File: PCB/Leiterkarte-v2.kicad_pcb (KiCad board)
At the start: 4 copper layers, 70 x 70 mm, 59 parts

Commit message: PCB Version 2.1
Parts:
- removed 3.3V1: LD39150DT33, Package_TO_SOT_SMD:TO-252-3_TabPin2
- removed Cmax1: 1nF, Capacitor_SMD:C_0805_2012Metric
- removed Rlind1, Rrind1, Rrpm1: 40k, Resistor_SMD:R_0603_1608Metric
- removed Rlind2, Rrind2, Rrpm2, Rspd1, Rup1: 10k, Resistor_SMD:R_0603_1608Metric
- removed Rspd2: 20k, Resistor_SMD:R_0603_1608Metric
- removed VRCond1: MAX9924UAUB_T, MAX9924UAUB:SOP50P490X110-10N
- added Cf1: spare, Capacitor_SMD:C_0805_2012Metric, F.Cu at (157.5, 91.5)
- added Cf10: C, Capacitor_SMD:C_0805_2012Metric, F.Cu at (124.0, 85.0)
- added Cf12: C, Capacitor_SMD:C_0805_2012Metric, F.Cu at (124.0, 88.0)
- added Cf13: C, Capacitor_SMD:C_0805_2012Metric, F.Cu at (124.0, 76.0)
- added Cf16: C, Capacitor_SMD:C_0805_2012Metric, F.Cu at (124.0, 79.0)
- added Cf3: spare, Capacitor_SMD:C_0805_2012Metric, F.Cu at (159.8, 91.5)
- added Cf5: C, Capacitor_SMD:C_0805_2012Metric, F.Cu at (125.0, 92.0)
- added Cf6: C, Capacitor_SMD:C_0805_2012Metric, F.Cu at (122.5, 92.0)
- added Cf8: C, Capacitor_SMD:C_0805_2012Metric, F.Cu at (124.0, 82.0)
- added Cin1.1: C, Capacitor_SMD:C_0805_2012Metric, F.Cu at (87.5, 99.0)
- added Cin2.1: C, Capacitor_SMD:C_0805_2012Metric, F.Cu at (101.0, 79.5)
- added Cout1.1: C, Capacitor_SMD:C_0805_2012Metric, F.Cu at (91.0, 73.0)
- added Cout2.1: C, Capacitor_SMD:C_0805_2012Metric, F.Cu at (102.5, 85.5)
- added D2: D_Schottky, Diode_SMD:D_0805_2012Metric, F.Cu at (159.8, 104.2)
- added D3: D_Schottky, Diode_SMD:D_0805_2012Metric, F.Cu at (159.0, 112.5)
- added D4: D_Schottky, Diode_SMD:D_0805_2012Metric, F.Cu at (159.0, 108.0)
- added D5: D_Zener 3.3V, Diode_SMD:D_0805_2012Metric, F.Cu at (170.0, 103.0)
- added D6: D_Schottky, Diode_SMD:D_0805_2012Metric, F.Cu at (163.8, 104.2)
- added D7: D_Zener 3.3V, Diode_SMD:D_0805_2012Metric, F.Cu at (157.5, 69.5)
- added D8: D_Zener 3.3V, Diode_SMD:D_0805_2012Metric, F.Cu at (157.5, 74.2)
- added JP1: SolderJumper_2_Open, Jumper:SolderJumper-2_P1.3mm_Open_TrianglePad1.0x1.5mm, F.Cu at (107.0, 57.5)
- added R10: 100k, Resistor_SMD:R_0805_2012Metric, F.Cu at (165.0, 112.5)
- added R11: 100k, Resistor_SMD:R_0805_2012Metric, F.Cu at (165.0, 108.0)
- added R12: spare, Resistor_SMD:R_0805_2012Metric, F.Cu at (162.0, 91.5)
- added R13: 10k, Resistor_SMD:R_0805_2012Metric, F.Cu at (167.2, 103.0)
- added R3: 100k, Resistor_SMD:R_0805_2012Metric, F.Cu at (157.6, 95.7)
- added R4: 10k, Resistor_SMD:R_0805_2012Metric, F.Cu at (160.4, 95.7)
- added R5: 10k, Resistor_SMD:R_0805_2012Metric, F.Cu at (173.8, 103.2)
- added R6: 10k, Resistor_SMD:R_0805_2012Metric, F.Cu at (161.0, 73.2)
- added R7: 10k, Resistor_SMD:R_0805_2012Metric, F.Cu at (161.1, 70.5)
- added R8: 40k, Resistor_SMD:R_0805_2012Metric, F.Cu at (164.6, 69.4)
- added R9: 40k, Resistor_SMD:R_0805_2012Metric, F.Cu at (164.6, 74.4)
- added TP1: TestPoint_Small, TestPoint:TestPoint_Pad_D1.0mm, F.Cu at (83.5, 101.2)
- added TP10: TestPoint_Small, TestPoint:TestPoint_Pad_D1.0mm, F.Cu at (162.0, 76.0)
- added TP11: TestPoint_Small, TestPoint:TestPoint_Pad_D1.0mm, F.Cu at (162.0, 67.5)
- added TP12: TestPoint_Small, TestPoint:TestPoint_Pad_D1.0mm, F.Cu at (164.2, 102.2)
- added TP13: TestPoint_Small, TestPoint:TestPoint_Pad_D1.0mm, F.Cu at (109.5, 60.2)
- added TP14: TestPoint_Small, TestPoint:TestPoint_Pad_D1.0mm, F.Cu at (109.5, 64.8)
- added TP15: TestPoint_Small, TestPoint:TestPoint_Pad_D1.0mm, F.Cu at (140.0, 99.5)
- added TP16: TestPoint_Small, TestPoint:TestPoint_Pad_D1.0mm, F.Cu at (142.5, 100.5)
- added TP18: TestPoint_Small, TestPoint:TestPoint_Pad_D1.0mm, F.Cu at (144.8, 97.8)
- added TP19: TestPoint_Small, TestPoint:TestPoint_Pad_D1.0mm, F.Cu at (148.2, 99.5)
- added TP20: TestPoint_Small, TestPoint:TestPoint_Pad_D1.0mm, F.Cu at (151.5, 101.0)
- added TP21: TestPoint_Small, TestPoint:TestPoint_Pad_D1.0mm, F.Cu at (145.0, 101.0)
- added TP22: TestPoint_Small, TestPoint:TestPoint_Pad_D1.0mm, F.Cu at (137.0, 100.5)
- added TP23: TestPoint_Small, TestPoint:TestPoint_Pad_D1.0mm, F.Cu at (134.8, 99.0)
- added TP24: TestPoint_Small, TestPoint:TestPoint_Pad_D1.0mm, F.Cu at (128.8, 63.5)
- added TP25: TestPoint_Small, TestPoint:TestPoint_Pad_D1.0mm, F.Cu at (136.2, 72.8)
- added TP26: TestPoint_Small, TestPoint:TestPoint_Pad_D1.0mm, F.Cu at (133.5, 62.8)
- added TP27: TestPoint_Small, TestPoint:TestPoint_Pad_D1.0mm, F.Cu at (135.8, 64.8)
- added TP28: TestPoint_Small, TestPoint:TestPoint_Pad_D1.0mm, F.Cu at (124.0, 64.5)
- added TP29: TestPoint_Small, TestPoint:TestPoint_Pad_D1.0mm, F.Cu at (132.0, 69.8)
- added TP3: TestPoint_Small, TestPoint:TestPoint_Pad_D1.0mm, F.Cu at (118.8, 99.2)
- added TP30: TestPoint_Small, TestPoint:TestPoint_Pad_D1.0mm, F.Cu at (155.2, 73.2)
- added TP31: TestPoint_Small, TestPoint:TestPoint_Pad_D1.0mm, F.Cu at (154.1, 70.4)
- added TP32: TestPoint_Small, TestPoint:TestPoint_Pad_D1.0mm, F.Cu at (158.8, 99.8)
- added TP33: TestPoint_Small, TestPoint:TestPoint_Pad_D1.0mm, F.Cu at (117.0, 80.5)
- added TP34: TestPoint_Small, TestPoint:TestPoint_Pad_D1.0mm, F.Cu at (163.0, 94.8)
- added TP35: TestPoint_Small, TestPoint:TestPoint_Pad_D1.0mm, F.Cu at (161.8, 100.0)
- added TP36: TestPoint_Small, TestPoint:TestPoint_Pad_D1.0mm, F.Cu at (152.2, 87.5)
- added TP37: TestPoint_Small, TestPoint:TestPoint_Pad_D1.0mm, F.Cu at (152.8, 52.8)
- added TP38: TestPoint_Small, TestPoint:TestPoint_Pad_D1.0mm, F.Cu at (164.0, 50.0)
- added TP39: TestPoint_Small, TestPoint:TestPoint_Pad_D1.0mm, F.Cu at (111.8, 90.2)
- added TP4: TestPoint_Small, TestPoint:TestPoint_Pad_D1.0mm, F.Cu at (105.8, 88.2)
- added TP5: TestPoint_Small, TestPoint:TestPoint_Pad_D1.0mm, F.Cu at (88.8, 77.2)
- added TP7: TestPoint_Small, TestPoint:TestPoint_Pad_D1.0mm, F.Cu at (170.0, 88.8)
- added TP8: TestPoint_Small, TestPoint:TestPoint_Pad_D1.0mm, F.Cu at (173.0, 88.8)
- added TP9: TestPoint_Small, TestPoint:TestPoint_Pad_D1.0mm, F.Cu at (176.0, 88.8)
- added U1: LMV321, LMV321SEG-7:SOT65P210X110-5N, F.Cu at (154.5, 93.8)
- added V3.31: LD39150DT33, Package_TO_SOT_SMD:TO-252-3_TabPin2, F.Cu at (95.0, 82.3)
- 5V1, Cboot1, Cin1, Cin2, Cout1, D1, L1, Rfbb1, Rfbt1: moved to F.Cu
- Fan1, Indics1, Speed1: footprint Connector_JST:JST_SH_BM02B-SRSS-TB_1x02-1MP_P1.00mm_Vertical -> Connector_JST:JST_XH_S2B-XH-A_1x02_P2.50mm_Horizontal
- R1, R2: value 10k -> 40k
- Rfuel1, Roil1: value 100 -> 240
- Rwtr1: value 100 -> 3k
- SPI1, SPI2, SPI3: footprint Connector_JST:JST_SH_BM08B-SRSS-TB_1x08-1MP_P1.00mm_Vertical -> Connector_JST:JST_XH_S8B-XH-A_1x08_P2.50mm_Horizontal
- TEMP_S1: value MCP9700Ax-ETT -> Conn_01x03_Pin; footprint Package_TO_SOT_SMD:SOT-23 -> Connector_JST:JST_XH_S3B-XH-A_1x03_P2.50mm_Horizontal
- TEMP_S2: value Conn_01x03_Pin -> MCP9700Ax-ETT; footprint Connector_JST:JST_SH_BM03B-SRSS-TB_1x03-1MP_P1.00mm_Vertical -> Package_TO_SOT_SMD:SOT-23
- gauges1: footprint Connector_JST:JST_SH_BM03B-SRSS-TB_1x03-1MP_P1.00mm_Vertical -> Connector_JST:JST_XH_S3B-XH-A_1x03_P2.50mm_Horizontal
- moved Resp1 52.5 mm to (147.5, 64.5), turned to 180 degrees
- moved Cen1 47.6 mm to (143.0, 70.5)
- moved ESP_RST1 46.5 mm to (141.5, 66.0)
- moved TEMP_S1 42.1 mm to (170.1, 64.8), turned to 90 degrees
- moved G*** 42.0 mm to (114.5, 69.5)
- moved Rboot1 39.5 mm to (130.5, 97.0), turned to -90 degrees
- moved ESP_BOOT1 33.0 mm to (124.5, 96.0)
- moved ESP1 30.8 mm to (139.5, 84.2)
- moved Fan1 29.9 mm to (170.1, 53.8), turned to 90 degrees
- moved Rbtn3 29.4 mm to (167.8, 93.8), turned to 90 degrees
- moved Cout1 29.3 mm to (94.0, 73.0)
- moved Rbtn1 27.9 mm to (170.2, 93.8), turned to 90 degrees
- moved Buttons1 27.2 mm to (177.8, 98.0), turned to -90 degrees
- moved RPM1 26.8 mm to (177.8, 102.0), turned to 0 degrees
- moved Cin2 26.2 mm to (101.0, 77.0), turned to 0 degrees
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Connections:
- ESP1 pad 17: LIndicator -> RIndicator
- ESP1 pad 18: RIndicator -> LIndicator
- ESP1 pad 19: Fuel -> WTemp
- ESP1 pad 21: WTemp -> Fuel
- R2 pad 2: Net-(VRCond1-IN+) -> GND
- Rbtn2 pad 1: Button2 -> GND
- Rbtn2 pad 2: GND -> Button3
- Rbtn3 pad 1: GND -> Button2
- Rbtn3 pad 2: Button3 -> GND
- TEMP_S1 pad 1: +3.3V -> GND
- TEMP_S1 pad 2: TEMP1 -> TEMP2
- TEMP_S1 pad 3: GND -> +3.3V
- TEMP_S2 pad 1: GND -> +3.3V
- TEMP_S2 pad 2: TEMP2 -> TEMP1
- TEMP_S2 pad 3: +3.3V -> GND
- USBC1 pad A4_B9: unconnected-(USBC1-VBUS-PadA4_B9) -> Net-(JP1-A)
- USBC1 pad B4_A9: unconnected-(USBC1-VBUS__1-PadB4_A9) -> Net-(JP1-A)
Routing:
- net +3.3V: track 263.5 -> 47.0 mm, vias 22 -> 16
- net GND: track 80.3 -> 164.5 mm, vias 40 -> 71
- net Net-(Cshld1-Pad2): track 0.00 -> 42.9 mm
- net Button3: track 61.1 -> 25.3 mm, vias 0 -> 1
- net USB_D-: track 15.8 -> 50.5 mm, vias 0 -> 2
- net USB_D+: track 17.0 -> 49.7 mm, vias 0 -> 2
- net Speed: track 57.7 -> 29.2 mm
- net Button2: track 75.1 -> 47.0 mm, vias 0 -> 2
- net BL: track 60.5 -> 88.1 mm
- net Net-(5V1-PH): track 15.9 -> 43.0 mm
- net Button1: track 74.6 -> 50.6 mm, vias 0 -> 2
- net CS3: track 33.9 -> 14.1 mm
- net Net-(D2-K): track 14.4 -> 31.2 mm, vias 2 -> 0
- net RST: track 68.4 -> 84.3 mm
- net Net-(5V1-VSENSE): track 4.71 -> 20.4 mm, vias 0 -> 2
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- added copper zone on B.Cu, net +3.3V
- added copper zone on F.Cu, net +3.3V
- removed copper zone on B.Cu, net GND
- removed copper zone on F.Cu, net GND
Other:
- board size 70 x 70 mm -> 100 x 70 mm
- board text added: "+"
- board text added: "3.3V"
- board text added: "5V"
- board text added: "BOOT"
- board text added: "Buttons"
- board text added: "FAN"
- board text added: "INDIC"
- board text added: "L"
- board text added: "O"
- board text added: "P"
- board text added: "R"
- board text added: "RPM"
- board text added: "Reset"
- board text added: "SPEED"
- board text added: "SPI1"
- board text added: "SPI2"
- board text added: "TEMP2"
- board text added: "VCC"
- board text added: "W"
- board text added: "v2.1 - XX.03.2025"
- board text removed: "+-"
- board text removed: "-+"
- board text removed: "-O+"
- board text removed: "FOW"
- board text removed: "LR"
- board text removed: "v2.0 - 12.10.2024"

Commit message: Fixed wrong SPI label
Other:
- board text added: "SPI3"
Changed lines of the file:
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@@
 		)
 	)
-	(gr_text "SPI2"
+	(gr_text "SPI3"
 		(at 143.75 103.25 0)
 		(layer "F.SilkS" knockout)
@@
 		(min_thickness 0.25)
 		(filled_areas_thickness no)
-		(fill yes
+		(fill
 			(thermal_gap 0.5)
 			(thermal_bridge_width 0.5)
@@
 		(min_thickness 0.25)
 		(filled_areas_thickness no)
-		(fill yes
+		(fill
 			(thermal_gap 0.5)
 			(thermal_bridge_width 0.5)

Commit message: Redone Schematics for better readability (the circuitry didnt change
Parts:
- removed 5V1: TPS5430DDA, Package_SO:TI_SO-PowerPAD-8_ThermalVias
- removed Buttons1: Conn_01x06_Pin, Connector_PinHeader_2.54mm:PinHeader_1x06_P2.54mm_Vertical
- removed Cboot1: 10nF, Capacitor_SMD:C_0805_2012Metric
- removed Cen1, Cin2: 1uF, Capacitor_SMD:C_0805_2012Metric
- removed Cesp1, Cin1: 22uF, Capacitor_SMD:C_0805_2012Metric
- removed Cesp2: 0.1uF, Capacitor_SMD:C_0805_2012Metric
- removed Cf1, Cf3: spare, Capacitor_SMD:C_0805_2012Metric
- removed Cf10, Cf12, Cf13, Cf16, Cf5, Cf6, Cf8, Cin1.1, Cin2.1, Cout1.1, Cout2.1: C, Capacitor_SMD:C_0805_2012Metric
- removed Cout1: 2.2uF, Capacitor_SMD:C_0805_2012Metric
- removed Cout2: 220uF, Capacitor_SMD:CP_Elec_6.3x5.9
- removed Cshld1: 50nF, Capacitor_SMD:C_0805_2012Metric
- removed D1: 550mV 5A, Diode_SMD:D_SMA
- removed D2, D3, D4, D6: D_Schottky, Diode_SMD:D_0805_2012Metric
- removed D5, D7, D8: D_Zener 3.3V, Diode_SMD:D_0805_2012Metric
- removed ESP1: ESP32-S3-WROOM-1U, RF_Module:ESP32-S3-WROOM-1U
- removed ESP_BOOT1, ESP_RST1: SW_SPST, button:small_button
- removed F1: 2A, Fuse:Fuse_1206_3216Metric
- removed Fan1, Indics1, Speed1: Conn_01x02_Pin, Connector_JST:JST_XH_S2B-XH-A_1x02_P2.50mm_Horizontal
- removed GND1, Vcc1: Conn_01x01_Pin, MountingHole:MountingHole_3.2mm_M3_Pad
- removed JP1: SolderJumper_2_Open, Jumper:SolderJumper-2_P1.3mm_Open_TrianglePad1.0x1.5mm
- removed L1: SPM6530T 15uH, SPM6530T:IND_SPM6530T-150M-HZ
- removed Qfan1: 2N7002-HXY, Package_TO_SOT_SMD:SOT-23
- removed R1, R2, R8, R9: 40k, Resistor_SMD:R_0805_2012Metric
- removed R10, R11, R3: 100k, Resistor_SMD:R_0805_2012Metric
- removed R12: spare, Resistor_SMD:R_0805_2012Metric
- removed R13, R4, R5, R6, R7: 10k, Resistor_SMD:R_0805_2012Metric
- removed RPM1: Conn_01x01_Pin, Connector_PinHeader_2.54mm:PinHeader_1x01_P2.54mm_Vertical
- removed Rboot1, Rbtn1, Rbtn2, Rbtn3, Rfbt1: 10k, Resistor_SMD:R_0603_1608Metric
- removed Resp1, Rusb1, Rusb2: 5.1k, Resistor_SMD:R_0603_1608Metric
- removed Rfbb1: 3.24k, Resistor_SMD:R_0603_1608Metric
- removed Rfuel1, Roil1: 240, Resistor_SMD:R_0603_1608Metric
- removed Rwtr1: 3k, Resistor_SMD:R_0603_1608Metric
- removed SD1: MSD-1-A, MSD-1-A:CUI_MSD-1-A
- removed SPI1, SPI2, SPI3: Conn_01x08, Connector_JST:JST_XH_S8B-XH-A_1x08_P2.50mm_Horizontal
- removed TEMP_S1, gauges1: Conn_01x03_Pin, Connector_JST:JST_XH_S3B-XH-A_1x03_P2.50mm_Horizontal
- removed TEMP_S2: MCP9700Ax-ETT, Package_TO_SOT_SMD:SOT-23
- removed TP1, TP10, TP11, TP12, TP13, TP14, TP15, TP16, TP18, TP19, TP20, TP21, TP22, TP23, TP24, TP25, TP26, TP27, TP28, TP29, TP3, TP30, TP31, TP32, TP33, TP34, TP35, TP36, TP37, TP38, TP39, TP4, TP5, TP7, TP8, TP9: TestPoint_Small, TestPoint:TestPoint_Pad_D1.0mm
- removed U1: LMV321, LMV321SEG-7:SOT65P210X110-5N
- removed USBC1: USB4105-GF-A, USB-C 2.0:GCT_USB4105-GF-A
- removed V3.31: LD39150DT33, Package_TO_SOT_SMD:TO-252-3_TabPin2
- added 5V301: TPS5430DDA, Package_SO:TI_SO-PowerPAD-8_ThermalVias, F.Cu at (94.1, 96.3)
- added Buttons601: Conn_01x06_Pin, Connector_PinHeader_2.54mm:PinHeader_1x06_P2.54mm_Vertical, F.Cu at (177.8, 98.0)
- added C401: C, Capacitor_SMD:C_0805_2012Metric, F.Cu at (122.5, 92.0)
- added C402: C, Capacitor_SMD:C_0805_2012Metric, F.Cu at (124.0, 79.0)
- added C403: C, Capacitor_SMD:C_0805_2012Metric, F.Cu at (124.0, 76.0)
- added C404: C, Capacitor_SMD:C_0805_2012Metric, F.Cu at (125.0, 92.0)
- added C405: C, Capacitor_SMD:C_0805_2012Metric, F.Cu at (124.0, 82.0)
- added C406: C, Capacitor_SMD:C_0805_2012Metric, F.Cu at (124.0, 85.0)
- added C407: C, Capacitor_SMD:C_0805_2012Metric, F.Cu at (124.0, 88.0)
- added C501: C, Capacitor_SMD:C_0805_2012Metric, F.Cu at (157.5, 91.5)
- added C502: C, Capacitor_SMD:C_0805_2012Metric, F.Cu at (159.8, 91.5)
- added Cboot301: 10nF, Capacitor_SMD:C_0805_2012Metric, F.Cu at (97.0, 89.0)
- added Cen201: 1uF, Capacitor_SMD:C_0805_2012Metric, F.Cu at (143.0, 70.5)
- added Cesp201: 22uF, Capacitor_SMD:C_0805_2012Metric, F.Cu at (147.5, 70.5)
- added Cesp202: 0.1uF, Capacitor_SMD:C_0805_2012Metric, F.Cu at (147.5, 67.5)
- added Cin301: C, Capacitor_SMD:C_0805_2012Metric, F.Cu at (101.0, 79.5)
- added Cin302: 1uF, Capacitor_SMD:C_0805_2012Metric, F.Cu at (101.0, 77.0)
- added Cin303: C, Capacitor_SMD:C_0805_2012Metric, F.Cu at (87.5, 99.0)
- added Cin304: 22uF, Capacitor_SMD:C_0805_2012Metric, F.Cu at (87.5, 96.5)
- added Cout301: 2.2uF, Capacitor_SMD:C_0805_2012Metric, F.Cu at (94.0, 73.0)
- added Cout302: C, Capacitor_SMD:C_0805_2012Metric, F.Cu at (91.0, 73.0)
- added Cout303: 220uF, Capacitor_SMD:CP_Elec_6.3x5.9, F.Cu at (109.5, 83.0)
- added Cout304: C, Capacitor_SMD:C_0805_2012Metric, F.Cu at (102.5, 85.5)
- added Cshld601: 50nF, Capacitor_SMD:C_0805_2012Metric, F.Cu at (137.0, 58.5)
- added D301: .55V 5A, Diode_SMD:D_SMA, F.Cu at (115.0, 97.2)
- added D401: Zener 3.3V, Diode_SMD:D_0805_2012Metric, F.Cu at (170.0, 103.0)
- added D402: Zener 3.3V, Diode_SMD:D_0805_2012Metric, F.Cu at (157.5, 74.2)
- added D403: Zener 3.3V, Diode_SMD:D_0805_2012Metric, F.Cu at (157.5, 69.5)
- added D501: D_Schottky, Diode_SMD:D_0805_2012Metric, F.Cu at (159.0, 108.0)
- added D502: D_Schottky, Diode_SMD:D_0805_2012Metric, F.Cu at (159.0, 112.5)
- added D503: D_Schottky, Diode_SMD:D_0805_2012Metric, F.Cu at (159.8, 104.2)
- added D504: D_Schottky, Diode_SMD:D_0805_2012Metric, F.Cu at (163.8, 104.2)
- added ESP201: ESP32-S3-WROOM-1U, RF_Module:ESP32-S3-WROOM-1U, F.Cu at (139.5, 84.2)
- added ESP_BOOT201: SW_SPST, button:small_button, F.Cu at (124.5, 96.0)
- added ESP_RST201: SW_SPST, button:small_button, F.Cu at (141.5, 66.0)
- added F301: 2A, Fuse:Fuse_1206_3216Metric, F.Cu at (87.0, 93.8)
- added Fan601: Conn_01x02_Pin, Connector_JST:JST_XH_S2B-XH-A_1x02_P2.50mm_Horizontal, F.Cu at (170.1, 53.8)
- added GND301: Conn_01x01_Pin, MountingHole:MountingHole_3.2mm_M3_Pad, F.Cu at (117.0, 87.0)
- added Indics401: Conn_01x02_Pin, Connector_JST:JST_XH_S2B-XH-A_1x02_P2.50mm_Horizontal, F.Cu at (170.1, 73.2)
- added JP601: SolderJumper_2_Open, Jumper:SolderJumper-2_P1.3mm_Open_TrianglePad1.0x1.5mm, F.Cu at (107.0, 57.5)
- added L301: SPM6530T 15uH, SPM6530T:IND_SPM6530T-150M-HZ, F.Cu at (106.2, 96.8)
- added Qfan601: 2N7002-HXY, Package_TO_SOT_SMD:SOT-23, F.Cu at (163.1, 53.7)
- added R401: 10k, Resistor_SMD:R_0805_2012Metric, F.Cu at (173.8, 103.2)
- added R402: 40k, Resistor_SMD:R_0805_2012Metric, F.Cu at (164.6, 74.4)
- added R403: 40k, Resistor_SMD:R_0805_2012Metric, F.Cu at (164.6, 69.4)
- added R404: 10k, Resistor_SMD:R_0805_2012Metric, F.Cu at (161.0, 73.2)
- added R405: 10k, Resistor_SMD:R_0805_2012Metric, F.Cu at (161.1, 70.5)
- added R406: 10k, Resistor_SMD:R_0805_2012Metric, F.Cu at (167.2, 103.0)
- added R501: 100k, Resistor_SMD:R_0805_2012Metric, F.Cu at (165.0, 108.0)
- added R502: 100k, Resistor_SMD:R_0805_2012Metric, F.Cu at (165.0, 112.5)
- added R503: 40k, Resistor_SMD:R_0805_2012Metric, F.Cu at (162.0, 108.0)
- added R504: 40k, Resistor_SMD:R_0805_2012Metric, F.Cu at (162.0, 112.5)
- added R505: R, Resistor_SMD:R_0805_2012Metric, F.Cu at (162.0, 91.5)
- added R506: 100k, Resistor_SMD:R_0805_2012Metric, F.Cu at (157.6, 95.7)
- added R507: 10k, Resistor_SMD:R_0805_2012Metric, F.Cu at (160.4, 95.7)
- added RPM401: Conn_01x01_Pin, Connector_PinHeader_2.54mm:PinHeader_1x01_P2.54mm_Vertical, F.Cu at (177.8, 102.0)
- added Rboot201: 10k, Resistor_SMD:R_0603_1608Metric, F.Cu at (130.5, 97.0)
- added Rbtn601: 10k, Resistor_SMD:R_0603_1608Metric, F.Cu at (170.2, 93.8)
- added Rbtn602: 10k, Resistor_SMD:R_0603_1608Metric, F.Cu at (167.8, 93.8)
- added Rbtn603: 10k, Resistor_SMD:R_0603_1608Metric, F.Cu at (165.2, 93.8)
- added Resp201: 5.1k, Resistor_SMD:R_0603_1608Metric, F.Cu at (147.5, 64.5)
- added Rfbb301: 3.24k, Resistor_SMD:R_0603_1608Metric, F.Cu at (100.5, 89.5)
- added Rfbt301: 10k, Resistor_SMD:R_0603_1608Metric, F.Cu at (103.5, 89.5)
- added Rfuel401: 240, Resistor_SMD:R_0603_1608Metric, F.Cu at (164.5, 84.2)
- added Roil401: 240, Resistor_SMD:R_0603_1608Metric, F.Cu at (164.5, 81.8)
- added Rusb601: 5.1k, Resistor_SMD:R_0603_1608Metric, F.Cu at (103.2, 58.0)
- added Rusb602: 5.1k, Resistor_SMD:R_0603_1608Metric, F.Cu at (97.2, 58.0)
- added Rwtr401: 3k, Resistor_SMD:R_0603_1608Metric, F.Cu at (164.5, 79.2)
- added SD601: MSD-1-A, MSD-1-A:CUI_MSD-1-A, F.Cu at (124.5, 52.5)
- added SPI601: Conn_01x08, Connector_JST:JST_XH_S8B-XH-A_1x08_P2.50mm_Horizontal, F.Cu at (88.0, 105.0)
- added SPI602: Conn_01x08, Connector_JST:JST_XH_S8B-XH-A_1x08_P2.50mm_Horizontal, F.Cu at (111.5, 105.0)
- added SPI603: Conn_01x08, Connector_JST:JST_XH_S8B-XH-A_1x08_P2.50mm_Horizontal, F.Cu at (135.0, 105.0)
- added Speed501: Conn_01x02_Pin, Connector_JST:JST_XH_S2B-XH-A_1x02_P2.50mm_Horizontal, F.Cu at (170.0, 111.5)
- added TEMP401: MCP9700Ax-ETT, Package_TO_SOT_SMD:SOT-23, F.Cu at (137.1, 69.6)
- added TEMP402: Conn_01x03_Pin, Connector_JST:JST_XH_S3B-XH-A_1x03_P2.50mm_Horizontal, F.Cu at (170.1, 64.8)
- added TP301: TestPoint_Small, TestPoint:TestPoint_Pad_D1.0mm, F.Cu at (83.5, 101.2)
- added TP302: TestPoint_Small, TestPoint:TestPoint_Pad_D1.0mm, F.Cu at (88.8, 77.2)
- added TP303: TestPoint_Small, TestPoint:TestPoint_Pad_D1.0mm, F.Cu at (105.8, 88.2)
- added TP304: TestPoint_Small, TestPoint:TestPoint_Pad_D1.0mm, F.Cu at (118.8, 99.2)
- added TP401: TestPoint_Small, TestPoint:TestPoint_Pad_D1.0mm, F.Cu at (162.0, 76.0)
- added TP402: TestPoint_Small, TestPoint:TestPoint_Pad_D1.0mm, F.Cu at (162.0, 67.5)
- added TP403: TestPoint_Small, TestPoint:TestPoint_Pad_D1.0mm, F.Cu at (155.2, 73.2)
- added TP404: TestPoint_Small, TestPoint:TestPoint_Pad_D1.0mm, F.Cu at (154.1, 70.4)
- added TP405: TestPoint_Small, TestPoint:TestPoint_Pad_D1.0mm, F.Cu at (164.2, 102.2)
- added TP406: TestPoint_Small, TestPoint:TestPoint_Pad_D1.0mm, F.Cu at (176.0, 88.8)
- added TP407: TestPoint_Small, TestPoint:TestPoint_Pad_D1.0mm, F.Cu at (173.0, 88.8)
- added TP408: TestPoint_Small, TestPoint:TestPoint_Pad_D1.0mm, F.Cu at (170.0, 88.8)
- added TP501: TestPoint_Small, TestPoint:TestPoint_Pad_D1.0mm, F.Cu at (158.8, 99.8)
- added TP502: TestPoint_Small, TestPoint:TestPoint_Pad_D1.0mm, F.Cu at (117.0, 80.5)
- added TP503: TestPoint_Small, TestPoint:TestPoint_Pad_D1.0mm, F.Cu at (161.8, 100.0)
- added TP504: TestPoint_Small, TestPoint:TestPoint_Pad_D1.0mm, F.Cu at (152.2, 87.5)
- added TP601: TestPoint_Small, TestPoint:TestPoint_Pad_D1.0mm, F.Cu at (128.8, 63.5)
- added TP602: TestPoint_Small, TestPoint:TestPoint_Pad_D1.0mm, F.Cu at (136.2, 72.8)
- added TP603: TestPoint_Small, TestPoint:TestPoint_Pad_D1.0mm, F.Cu at (133.5, 62.8)
- added TP604: TestPoint_Small, TestPoint:TestPoint_Pad_D1.0mm, F.Cu at (135.8, 64.8)
- added TP605: TestPoint_Small, TestPoint:TestPoint_Pad_D1.0mm, F.Cu at (124.0, 64.5)
- added TP606: TestPoint_Small, TestPoint:TestPoint_Pad_D1.0mm, F.Cu at (132.0, 69.8)
- added TP607: TestPoint_Small, TestPoint:TestPoint_Pad_D1.0mm, F.Cu at (109.5, 64.8)
- added TP608: TestPoint_Small, TestPoint:TestPoint_Pad_D1.0mm, F.Cu at (109.5, 60.2)
- added TP609: TestPoint_Small, TestPoint:TestPoint_Pad_D1.0mm, F.Cu at (140.0, 99.5)
- added TP610: TestPoint_Small, TestPoint:TestPoint_Pad_D1.0mm, F.Cu at (152.8, 52.8)
- added TP611: TestPoint_Small, TestPoint:TestPoint_Pad_D1.0mm, F.Cu at (142.5, 100.5)
- added TP612: TestPoint_Small, TestPoint:TestPoint_Pad_D1.0mm, F.Cu at (144.8, 97.8)
- added TP613: TestPoint_Small, TestPoint:TestPoint_Pad_D1.0mm, F.Cu at (148.2, 99.5)
- added TP614: TestPoint_Small, TestPoint:TestPoint_Pad_D1.0mm, F.Cu at (151.5, 101.0)
- added TP615: TestPoint_Small, TestPoint:TestPoint_Pad_D1.0mm, F.Cu at (164.0, 50.0)
- added TP616: TestPoint_Small, TestPoint:TestPoint_Pad_D1.0mm, F.Cu at (145.0, 101.0)
- added TP617: TestPoint_Small, TestPoint:TestPoint_Pad_D1.0mm, F.Cu at (137.0, 100.5)
- added TP618: TestPoint_Small, TestPoint:TestPoint_Pad_D1.0mm, F.Cu at (111.8, 90.2)
- added TP619: TestPoint_Small, TestPoint:TestPoint_Pad_D1.0mm, F.Cu at (134.8, 99.0)
- added U501: LMV321, LMV321SEG-7:SOT65P210X110-5N, F.Cu at (154.5, 93.8)
- added USBC601: USB4105-GF-A, USB-C 2.0:GCT_USB4105-GF-A, F.Cu at (100.5, 48.0)
- added V301: LD39150DT33, Package_TO_SOT_SMD:TO-252-3_TabPin2, F.Cu at (95.0, 82.3)
- added Vcc301: Conn_01x01_Pin, MountingHole:MountingHole_3.2mm_M3_Pad, F.Cu at (85.5, 87.0)
- added gauges401: Conn_01x03_Pin, Connector_JST:JST_XH_S3B-XH-A_1x03_P2.50mm_Horizontal, F.Cu at (170.1, 84.2)
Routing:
- net BL: track 88.1 -> 0.00 mm
- net /MCU/BL: track 0.00 -> 88.1 mm
- net RST: track 84.3 -> 0.00 mm, vias 4 -> 0
- net /MCU/RST: track 0.00 -> 84.3 mm, vias 0 -> 4
- net DC: track 79.4 -> 0.00 mm, vias 4 -> 0
- net /MCU/DC: track 0.00 -> 79.4 mm, vias 0 -> 4
- net CLK: track 72.5 -> 0.00 mm, vias 4 -> 0
- net /MCU/CLK: track 0.00 -> 72.5 mm, vias 0 -> 4
- net DIN: track 68.7 -> 0.00 mm, vias 4 -> 0
- net /MCU/DIN: track 0.00 -> 68.7 mm, vias 0 -> 4
- net RPM: track 63.6 -> 0.00 mm, vias 2 -> 0
- net /MCU/RPM: track 0.00 -> 63.6 mm, vias 0 -> 2
- net WTemp: track 61.9 -> 0.00 mm
- net /MCU/WTemp: track 0.00 -> 61.9 mm
- net Oil: track 57.7 -> 0.00 mm
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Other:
- board text added: "F"
- board text removed: "P"

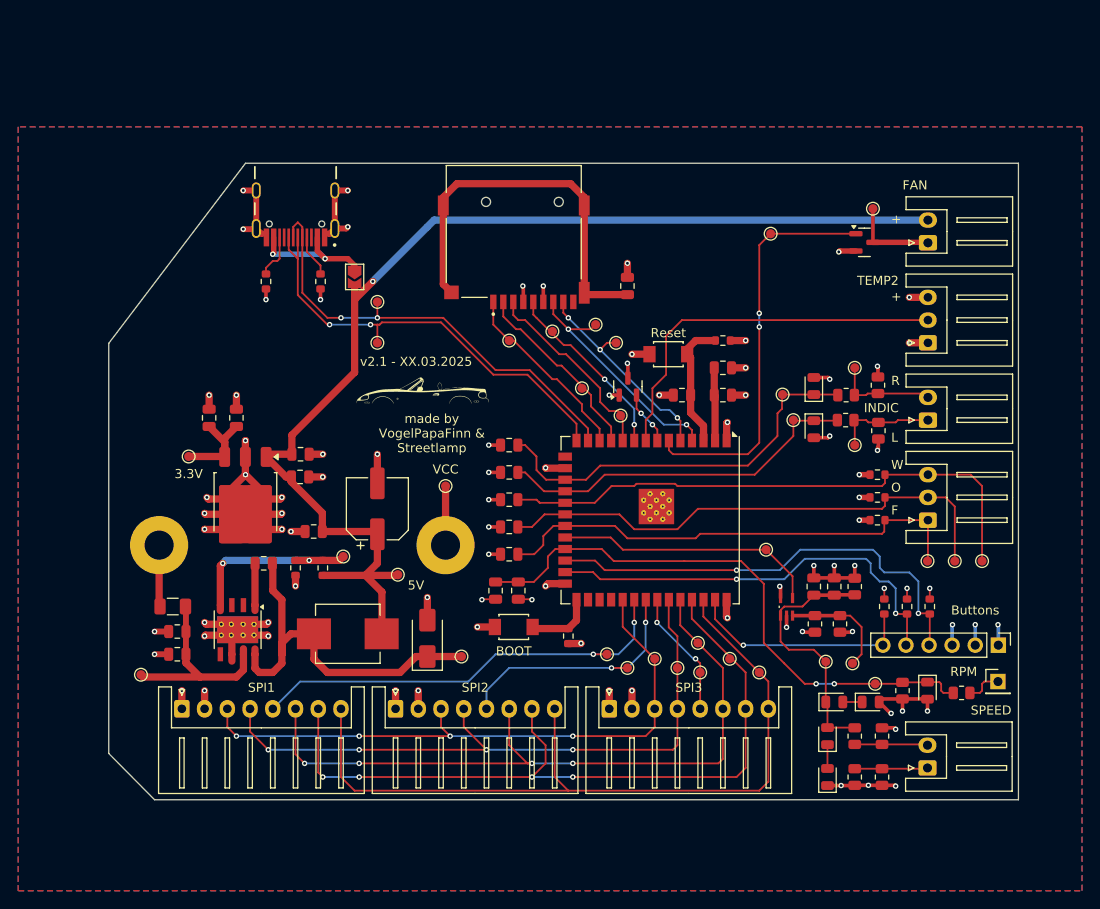
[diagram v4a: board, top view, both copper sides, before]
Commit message: Applied recommendations from my coworker; Fixed badly placed filter caps; Added flyback diode to fan circuit; Applied larger grid and some spacing to the schematics; And some other small adjustments
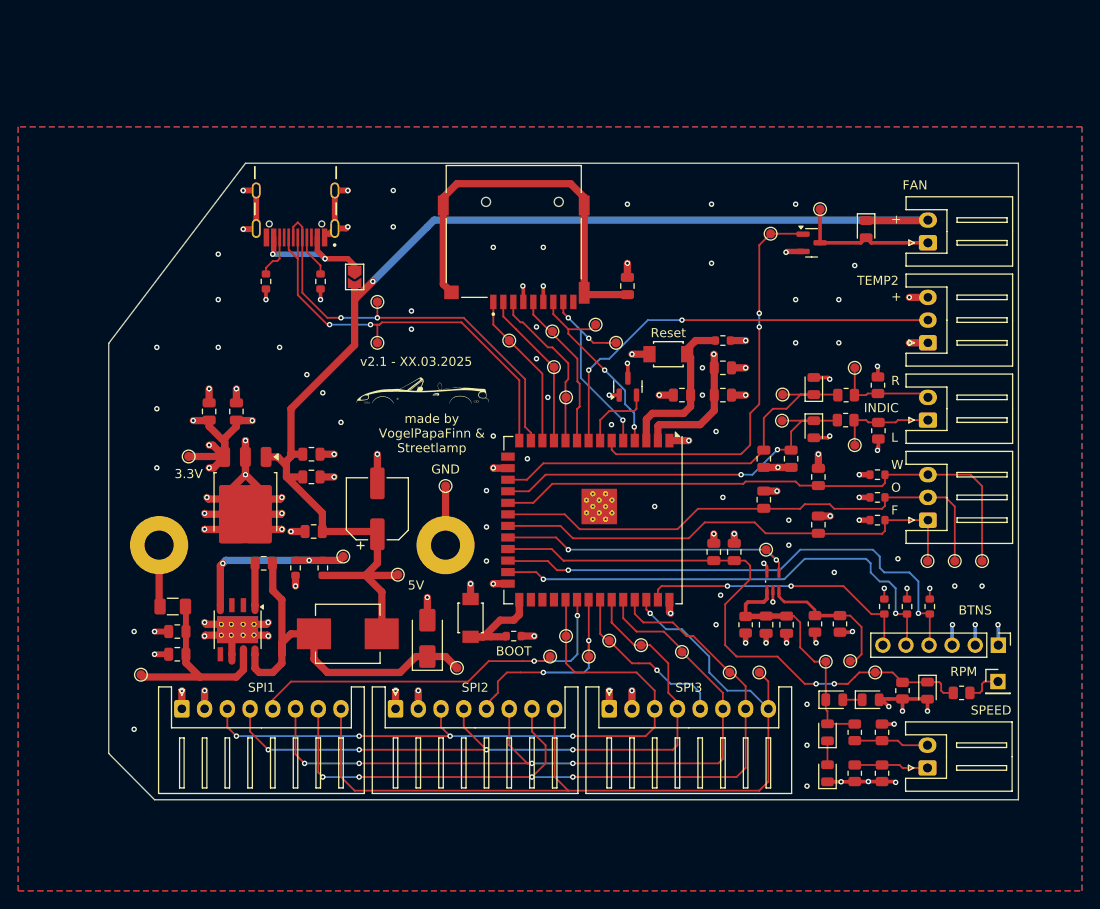
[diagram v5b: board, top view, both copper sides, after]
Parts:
- added D601: D_Schottky, Diode_SMD:D_0805_2012Metric, F.Cu at (163.2, 52.2)
- moved C407 34.2 mm to (158.0, 84.8), turned to 90 degrees
- moved C405 34.1 mm to (158.0, 79.5), turned to 90 degrees
- moved C402 31.0 mm to (155.0, 77.5), turned to -90 degrees
- moved C406 28.2 mm to (152.0, 82.0), turned to 90 degrees
- moved C403 28.0 mm to (152.0, 77.5), turned to 90 degrees
- moved C401 24.4 mm to (146.5, 87.8), turned to -90 degrees
- moved C404 24.1 mm to (148.8, 87.8), turned to 90 degrees
- moved R505 12.7 mm to (150.0, 95.8), turned to -90 degrees
- moved TP616 10.6 mm to (135.0, 97.5)
- moved TP609 10.1 mm to (130.2, 97.0)
- moved C502 8.60 mm to (152.2, 95.8), turned to -90 degrees
- moved TP602 6.32 mm to (130.2, 70.8)
- moved ESP201 6.29 mm to (133.2, 84.2)
- moved TP619 6.25 mm to (128.5, 99.2)
- moved Rboot201 6.00 mm to (124.5, 97.0), turned to 180 degrees
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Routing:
- net +3.3V: track 47.0 -> 62.8 mm, vias 16 -> 21
- net GND: track 164.5 -> 154.9 mm, vias 71 -> 122
- net /MCU/BL: track 88.1 -> 97.6 mm, vias 0 -> 1
- net +5V: track 128.9 -> 137.8 mm
- net /MCU/DIN: track 68.7 -> 75.3 mm
- net /MCU/Button1: track 50.6 -> 57.2 mm
- net Net-(D601-A): track 9.72 -> 16.2 mm
- net /MCU/Button2: track 47.0 -> 53.3 mm
- net /MCU/Button3: track 25.3 -> 30.9 mm, vias 1 -> 2
- net /MCU/TEMP2: track 41.9 -> 47.3 mm, vias 0 -> 2
- net /MCU/CS2: track 28.6 -> 23.4 mm
- net /MCU/RST: track 84.3 -> 89.4 mm
- net /MCU/CS3: track 14.1 -> 19.2 mm, vias 2 -> 1
- net /MCU/Speed: track 29.2 -> 33.7 mm, vias 0 -> 2
- net Net-(ESP201-IO0): track 7.55 -> 12.0 mm
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- added copper zone on In2.Cu, net +3.3V
- added copper zone on B.Cu, net GND
- added copper zone on F.Cu, net GND
- removed copper zone on B.Cu, net +3.3V
- removed copper zone on F.Cu, net +3.3V
- removed copper zone on In2.Cu, net GND
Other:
- board text added: "BTNS"
- board text added: "GND"
- board text removed: "Buttons"
- board text removed: "VCC"
